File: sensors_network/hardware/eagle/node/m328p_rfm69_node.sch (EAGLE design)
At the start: 36 parts, among them IC2 L6920, SW2 Node ID, U1 M328P, U2 RFM69W, Y1 8MHz

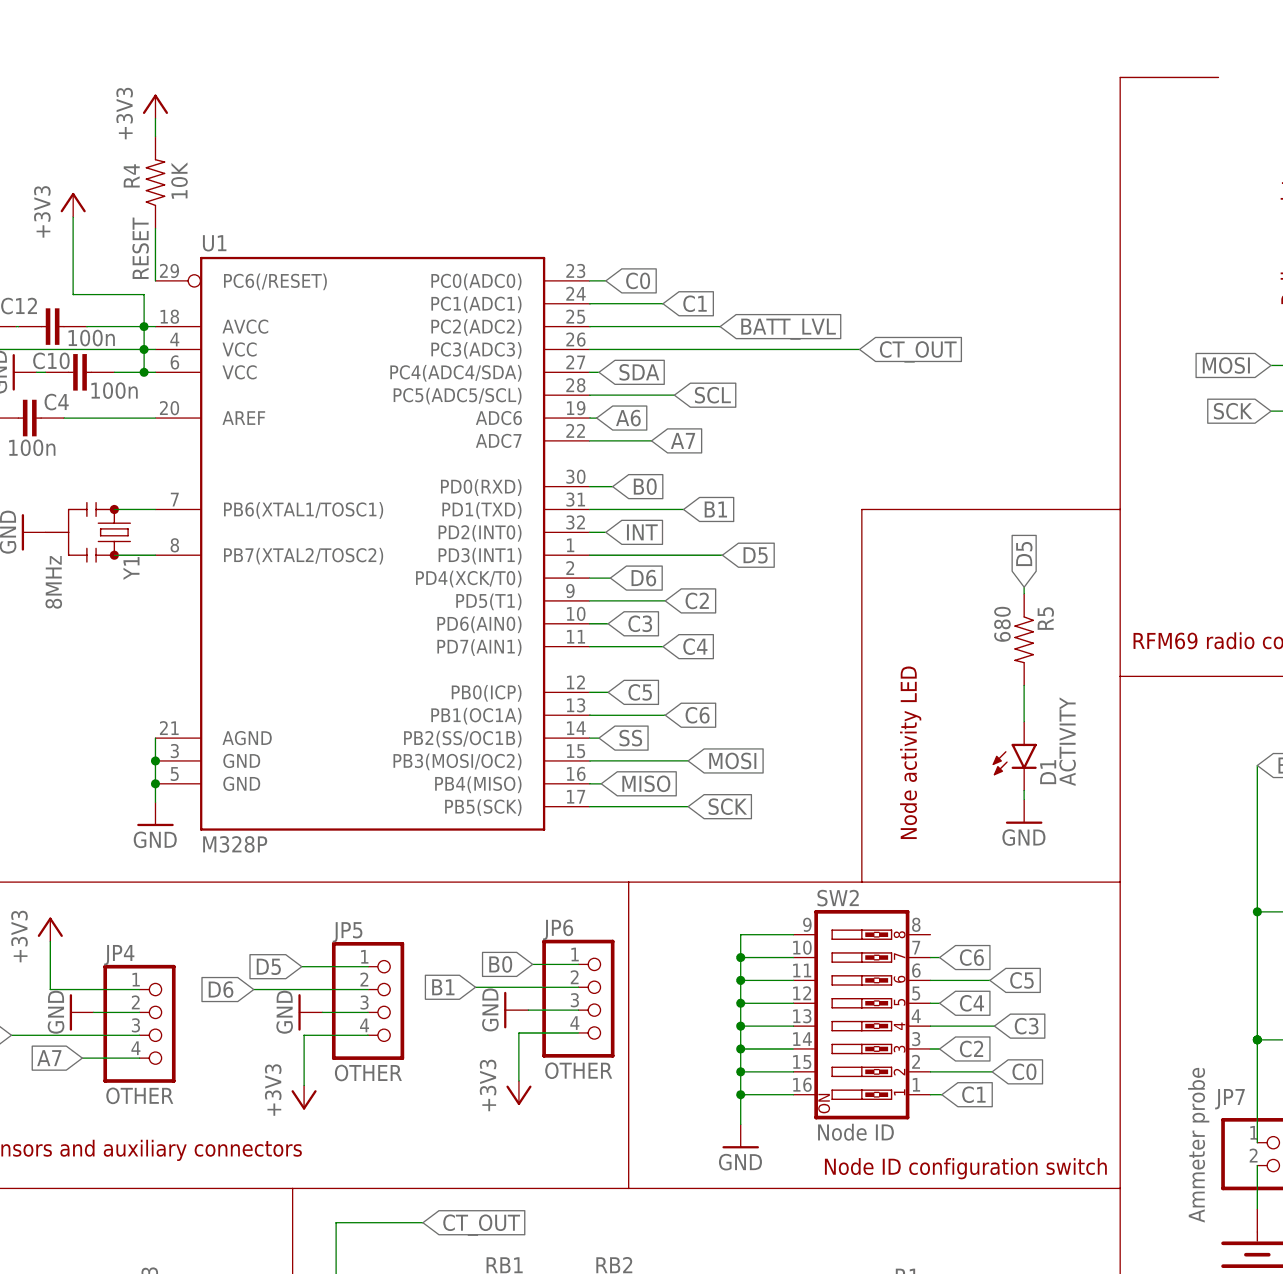
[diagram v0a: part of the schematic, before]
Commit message: [sensors_network] pcb - added necessary text and infos
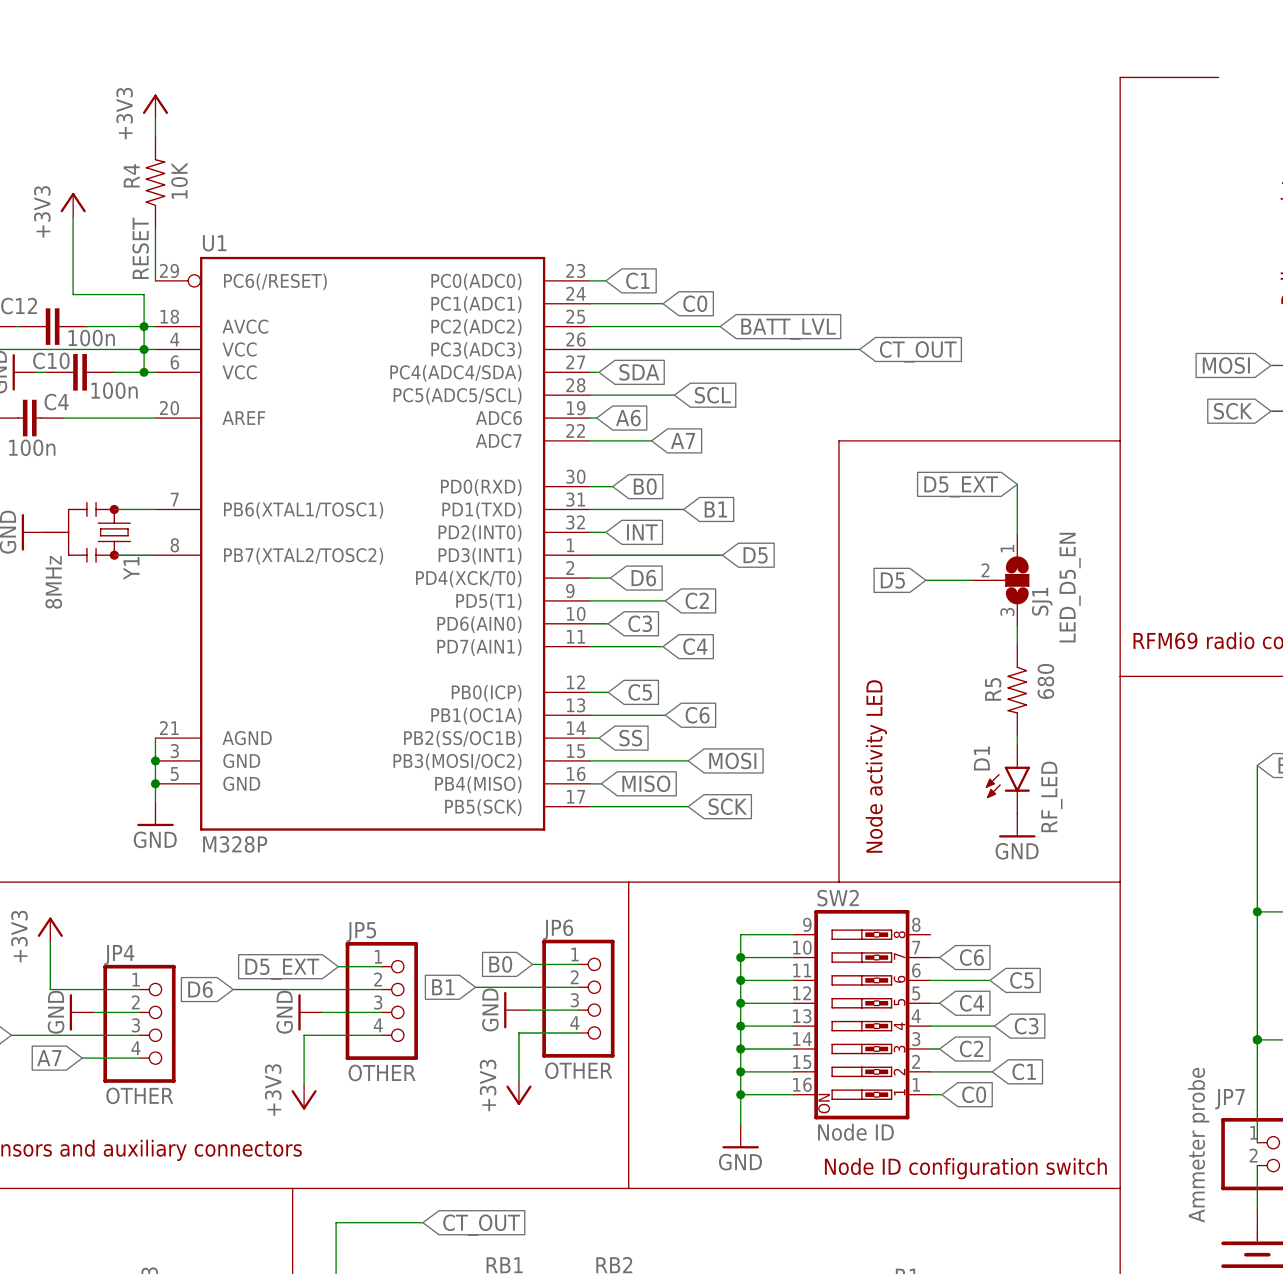
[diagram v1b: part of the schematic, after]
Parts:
- added SJ1: LED_D5_EN, jumper:SJ2W
- D1: value ACTIVITY -> RF_LED
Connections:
- new net D5_EXT: JP5.1, SJ1.1
- new net N$13: R5.1, SJ1.3
- net C0: now also SW2.1, U1.PC1(ADC1); no longer SW2.2, U1.PC0(ADC0)
- net C1: now also SW2.2, U1.PC0(ADC0); no longer SW2.1, U1.PC1(ADC1)
- net D5: now also SJ1.2; no longer JP5.1, R5.1
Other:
- moved on the sheet: D1, JP5, R5
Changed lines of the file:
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@@
 <setting verticaltext="up"/>
 </settings>
-<grid distance="0.1" unitdist="inch" unit="inch" style="lines" multiple="1" display="no" altdistance="0.01" altunitdist="inch" altunit="inch"/>
+<grid distance="0.01" unitdist="inch" unit="inch" style="dots" multiple="1" display="yes" altdistance="0.01" altunitdist="inch" altunit="inch"/>
 <layers>
 <layer number="1" name="Top" color="4" fill="1" visible="no" active="no"/>
@@
 <part name="GND24" library="supply1" deviceset="GND" device=""/>
 <part name="JP7" library="pinhead" deviceset="PINHD-1X2" device="" value="Ammeter probe"/>
-<part name="D1" library="SparkFun-LED" deviceset="LED" device="0603" value="ACTIVITY"/>
+<part name="D1" library="SparkFun-LED" deviceset="LED" device="0603" value="RF_LED"/>
 <part name="R5" library="SparkFun-Passives" deviceset="RESISTOR" device="0805-RES" value="680"/>
 <part name="GND25" library="supply1" deviceset="GND" device=""/>
+<part name="SJ1" library="jumper" deviceset="SJ2W" device="" value="LED_D5_EN"/>
 </parts>
 <sheets>
@@
 <plain>
 <wire x1="172.212" y1="175.26" x2="161.29" y2="175.26" width="0.1524" layer="94"/>
-<wire x1="161.29" y1="175.26" x2="161.29" y2="127.254" width="0.1016" layer="94"/>
-<wire x1="161.29" y1="127.254" x2="161.29" y2="108.712" width="0.1016" layer="94"/>
+<wire x1="161.29" y1="175.26" x2="161.29" y2="134.874" width="0.1016" layer="94"/>
+<wire x1="161.29" y1="134.874" x2="161.29" y2="108.712" width="0.1016" layer="94"/>
 <wire x1="161.29" y1="108.712" x2="256.54" y2="108.712" width="0.1016" layer="94"/>
 <wire x1="161.29" y1="24.13" x2="161.29" y2="51.816" width="0.1016" layer="94"/>
@@
 <wire x1="106.68" y1="51.816" x2="161.29" y2="51.816" width="0.1016" layer="94"/>
 <wire x1="4.064" y1="85.852" x2="106.68" y2="85.852" width="0.1016" layer="94"/>
-<wire x1="106.68" y1="85.852" x2="132.588" y2="85.852" width="0.1016" layer="94"/>
-<wire x1="132.588" y1="85.852" x2="161.29" y2="85.852" width="0.1016" layer="94"/>
+<wire x1="106.68" y1="85.852" x2="130.048" y2="85.852" width="0.1016" layer="94"/>
+<wire x1="130.048" y1="85.852" x2="161.29" y2="85.852" width="0.1016" layer="94"/>
 <wire x1="69.342" y1="3.81" x2="69.342" y2="51.816" width="0.1016" layer="94"/>
 <text x="12.7" y="9.144" size="1.778" layer="94">In System Programming</text>
@@
 <wire x1="106.68" y1="85.852" x2="106.68" y2="51.816" width="0.1016" layer="94"/>
 <text x="128.27" y="53.34" size="1.778" layer="94">Node ID configuration switch</text>
-<wire x1="161.29" y1="127.254" x2="132.588" y2="127.254" width="0.1016" layer="94"/>
-<wire x1="132.588" y1="127.254" x2="132.588" y2="85.852" width="0.1016" layer="94"/>
-<text x="138.684" y="90.424" size="1.778" layer="94" rot="R90">Node activity LED</text>
+<wire x1="161.29" y1="134.874" x2="130.048" y2="134.874" width="0.1016" layer="94"/>
+<wire x1="130.048" y1="134.874" x2="130.048" y2="85.852" width="0.1016" layer="94"/>
+<text x="134.874" y="88.9" size="1.778" layer="94" rot="R90">Node activity LED</text>
 </plain>
 <instances>
@@
 </instance>
 <instance part="U1" gate="U$1" x="79.502" y="122.174"/>
-<instance part="JP5" gate="A" x="80.264" y="71.374"/>
+<instance part="JP5" gate="A" x="81.788" y="71.374"/>
 <instance part="JP6" gate="A" x="103.632" y="71.628"/>
 <instance part="GND21" gate="1" x="70.104" y="71.374" rot="R270"/>
@@
 <attribute name="VALUE" x="170.688" y="48.006" size="1.778" layer="96" rot="R90"/>
 </instance>
-<instance part="D1" gate="G$1" x="150.622" y="101.092"/>
-<instance part="R5" gate="G$1" x="150.622" y="112.776" rot="R270"/>
-<instance part="GND25" gate="1" x="150.622" y="92.456"/>
+<instance part="D1" gate="G$1" x="149.86" y="98.552" smashed="yes">
+<attribute name="NAME" x="146.812" y="98.044" size="1.778" layer="95" rot="R90"/>
+<attribute name="VALUE" x="154.305" y="91.186" size="1.778" layer="96" rot="R90"/>
+</instance>
+<instance part="R5" gate="G$1" x="149.86" y="107.188" smashed="yes" rot="R270">
+<attribute name="NAME" x="146.2786" y="108.712" size="1.778" layer="95" rot="R270"/>
+<attribute name="VALUE" x="152.146" y="110.236" size="1.778" layer="96" rot="R270"/>
+</instance>
+<instance part="GND25" gate="1" x="149.86" y="90.932"/>
+<instance part="SJ1" gate="G$1" x="149.86" y="119.38" smashed="yes">
+<attribute name="NAME" x="153.289" y="115.316" size="1.778" layer="95" rot="R90"/>
+<attribute name="VALUE" x="156.337" y="112.268" size="1.778" layer="96" rot="R90"/>
+</instance>
 </instances>
 <busses>
@@
 <segment>
 <pinref part="JP5" gate="A" pin="3"/>
-<wire x1="77.724" y1="71.374" x2="72.644" y2="71.374" width="0.1524" layer="91"/>
+<wire x1="79.248" y1="71.374" x2="72.644" y2="71.374" width="0.1524" layer="91"/>
 <pinref part="GND21" gate="1" pin="GND"/>
 </segment>
@@
 <pinref part="D1" gate="G$1" pin="C"/>
 <pinref part="GND25" gate="1" pin="GND"/>
-<wire x1="150.622" y1="94.996" x2="150.622" y2="96.012" width="0.1524" layer="91"/>
 </segment>
 </net>
@@
 <segment>
 <pinref part="JP5" gate="A" pin="4"/>
-<wire x1="77.724" y1="68.834" x2="70.612" y2="68.834" width="0.1524" layer="91"/>
+<wire x1="79.248" y1="68.834" x2="70.612" y2="68.834" width="0.1524" layer="91"/>
 <wire x1="70.612" y1="68.834" x2="70.612" y2="63.246" width="0.1524" layer="91"/>
 <pinref part="+3V10" gate="G$1" pin="+3V3"/>
@@
 <net name="D5" class="0">
 <segment>
-<pinref part="JP5" gate="A" pin="1"/>
-<wire x1="77.724" y1="76.454" x2="70.358" y2="76.454" width="0.1524" layer="91"/>
-<label x="70.358" y="76.454" size="1.778" layer="95" rot="R180" xref="yes"/>
-</segment>
-<segment>
 <pinref part="U1" gate="U$1" pin="PD3(INT1)"/>
 <wire x1="102.362" y1="122.174" x2="117.094" y2="122.174" width="0.1524" layer="91"/>
@@
 </segment>
 <segment>
-<pinref part="R5" gate="G$1" pin="1"/>
-<wire x1="150.622" y1="117.856" x2="150.622" y2="118.618" width="0.1524" layer="91"/>
-<label x="150.622" y="118.618" size="1.778" layer="95" rot="R90" xref="yes"/>
+<pinref part="SJ1" gate="G$1" pin="2"/>
+<wire x1="144.78" y1="119.38" x2="139.7" y2="119.38" width="0.1524" layer="91"/>
+<label x="139.7" y="119.38" size="1.778" layer="95" rot="R180" xref="yes"/>
 </segment>
 </net>
@@
 <segment>
 <pinref part="JP5" gate="A" pin="2"/>
-<wire x1="77.724" y1="73.914" x2="65.024" y2="73.914" width="0.1524" layer="91"/>
-<label x="65.024" y="73.914" size="1.778" layer="95" rot="R180" xref="yes"/>
+<wire x1="79.248" y1="73.914" x2="62.738" y2="73.914" width="0.1524" layer="91"/>
+<label x="62.738" y="73.914" size="1.778" layer="95" rot="R180" xref="yes"/>
 </segment>
 <segment>
@@
 <net name="C1" class="0">
 <segment>
+<wire x1="102.362" y1="152.654" x2="104.14" y2="152.654" width="0.1524" layer="91"/>
+<label x="104.14" y="152.654" size="1.778" layer="95" xref="yes"/>
+<pinref part="U1" gate="U$1" pin="PC0(ADC0)"/>
+</segment>
+<segment>
+<pinref part="SW2" gate="A" pin="2"/>
+<wire x1="140.208" y1="64.77" x2="147.066" y2="64.77" width="0.1524" layer="91"/>
+<label x="147.066" y="64.77" size="1.778" layer="95" xref="yes"/>
+</segment>
+</net>
+<net name="C0" class="0">
+<segment>
+<wire x1="102.362" y1="150.114" x2="110.49" y2="150.114" width="0.1524" layer="91"/>
+<label x="110.49" y="150.114" size="1.778" layer="95" xref="yes"/>
+<pinref part="U1" gate="U$1" pin="PC1(ADC1)"/>
+</segment>
+<segment>
 <pinref part="SW2" gate="A" pin="1"/>
 <wire x1="140.208" y1="62.23" x2="141.478" y2="62.23" width="0.1524" layer="91"/>
 <label x="141.478" y="62.23" size="1.778" layer="95" xref="yes"/>
 </segment>
-<segment>
-<wire x1="102.362" y1="150.114" x2="110.49" y2="150.114" width="0.1524" layer="91"/>
-<label x="110.49" y="150.114" size="1.778" layer="95" xref="yes"/>
-<pinref part="U1" gate="U$1" pin="PC1(ADC1)"/>
-</segment>
-</net>
-<net name="C0" class="0">
-<segment>
-<pinref part="SW2" gate="A" pin="2"/>
-<wire x1="140.208" y1="64.77" x2="147.066" y2="64.77" width="0.1524" layer="91"/>
-<label x="147.066" y="64.77" size="1.778" layer="95" xref="yes"/>
-</segment>
-<segment>
-<wire x1="102.362" y1="152.654" x2="104.14" y2="152.654" width="0.1524" layer="91"/>
-<label x="104.14" y="152.654" size="1.778" layer="95" xref="yes"/>
-<pinref part="U1" gate="U$1" pin="PC0(ADC0)"/>
-</segment>
 </net>
 <net name="A6" class="0">
@@
 <pinref part="R5" gate="G$1" pin="2"/>
 <pinref part="D1" gate="G$1" pin="A"/>
-<wire x1="150.622" y1="103.632" x2="150.622" y2="107.696" width="0.1524" layer="91"/>
-</segment>
-</net>
+<wire x1="149.86" y1="101.092" x2="149.86" y2="102.108" width="0.1524" layer="91"/>
+</segment>
+</net>
+<net name="N$13" class="0">
+<segment>
+<pinref part="SJ1" gate="G$1" pin="3"/>
+<pinref part="R5" gate="G$1" pin="1"/>
+<wire x1="149.86" y1="112.268" x2="149.86" y2="114.3" width="0.1524" layer="91"/>
+</segment>
+</net>
+<net name="D5_EXT" class="0">
+<segment>
+<pinref part="SJ1" gate="G$1" pin="1"/>
+<wire x1="149.86" y1="124.46" x2="149.86" y2="130.048" width="0.1524" layer="91"/>
+<label x="149.86" y="130.048" size="1.778" layer="95" rot="R180" xref="yes"/>
+</segment>
+<segment>
+<pinref part="JP5" gate="A" pin="1"/>
+<wire x1="79.248" y1="76.454" x2="74.422" y2="76.454" width="0.1524" layer="91"/>
+<label x="74.422" y="76.454" size="1.778" layer="95" rot="R180" xref="yes"/>
+</segment>
+</net>
